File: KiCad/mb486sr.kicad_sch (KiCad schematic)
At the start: 0 parts

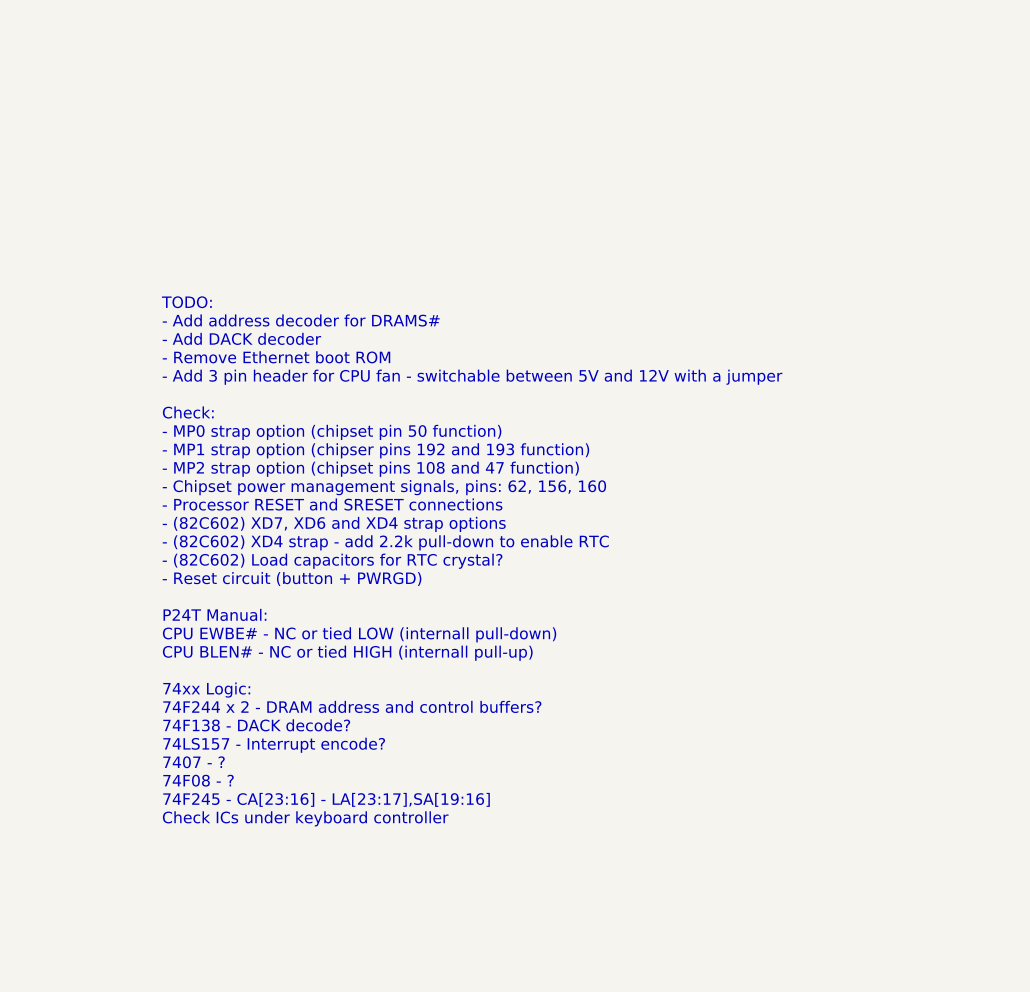
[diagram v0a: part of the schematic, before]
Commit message: Version 0.2: Update cache schematic
Signed-off-by: Sergey Kiselev <sergey.kiselev@intel.com>
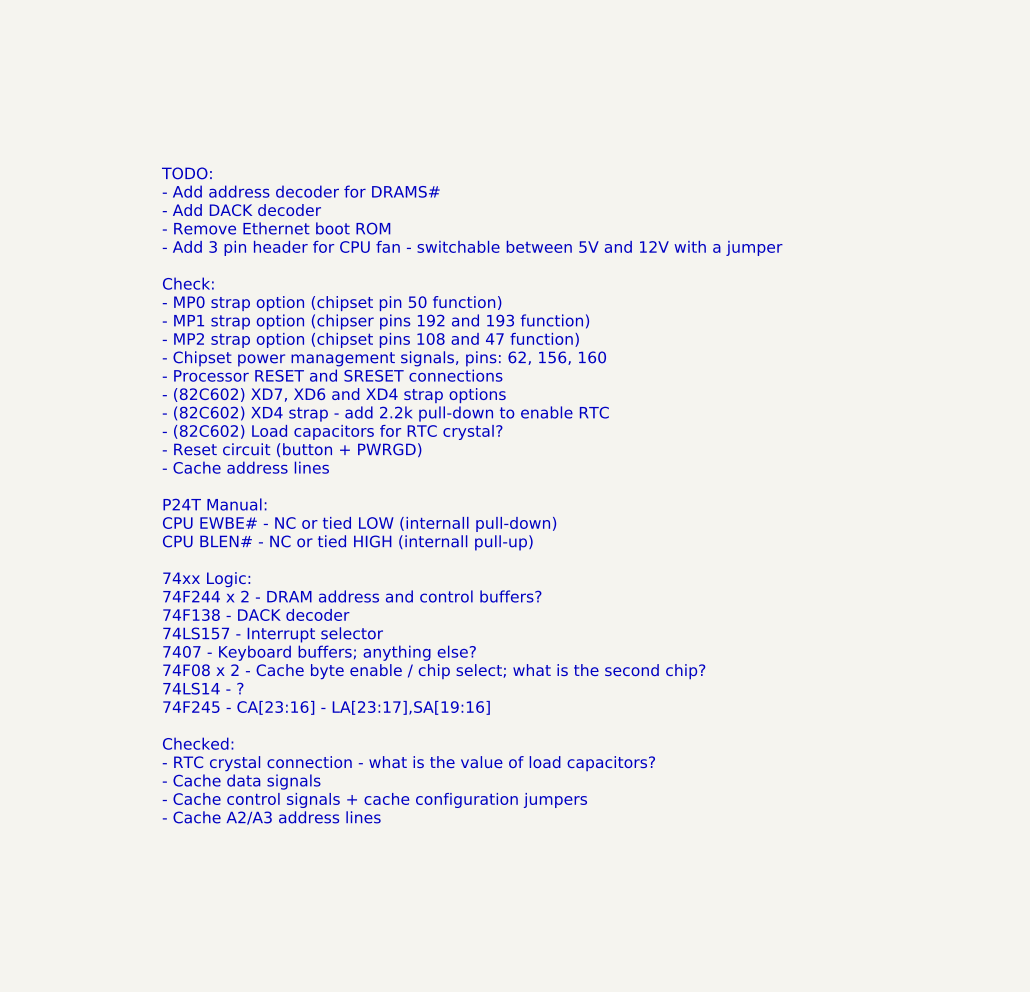
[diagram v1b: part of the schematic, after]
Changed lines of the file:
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@@
     (title "486 Sandy River Motherboard")
   )
-  (text "TODO:\n- Add address decoder for DRAMS#\n- Add DACK decoder\n- Remove Ethernet boot ROM\n- Add 3 pin header for CPU fan - switchable between 5V and 12V with a jumper\n\nCheck:\n- MP0 strap option (chipset pin 50 function)\n- MP1 strap option (chipser pins 192 and 193 function)\n- MP2 strap option (chipset pins 108 and 47 function)\n- Chipset power management signals, pins: 62, 156, 160\n- Processor RESET and SRESET connections\n- (82C602) XD7, XD6 and XD4 strap options \n- (82C602) XD4 strap - add 2.2k pull-down to enable RTC\n- (82C602) Load capacitors for RTC crystal?\n- Reset circuit (button + PWRGD)\n\nP24T Manual:\nCPU EWBE# - NC or tied LOW (internall pull-down)\nCPU BLEN# - NC or tied HIGH (internall pull-up)\n\n74xx Logic:\n74F244 x 2 - DRAM address and control buffers?\n74F138 - DACK decode?\n74LS157 - Interrupt encode?\n7407 - ?\n74F08 - ?\n74F245 - CA[23:16] - LA[23:17],SA[19:16]\nCheck ICs under keyboard controller"
+  (text "TODO:\n- Add address decoder for DRAMS#\n- Add DACK decoder\n- Remove Ethernet boot ROM\n- Add 3 pin header for CPU fan - switchable between 5V and 12V with a jumper\n\nCheck:\n- MP0 strap option (chipset pin 50 function)\n- MP1 strap option (chipser pins 192 and 193 function)\n- MP2 strap option (chipset pins 108 and 47 function)\n- Chipset power management signals, pins: 62, 156, 160\n- Processor RESET and SRESET connections\n- (82C602) XD7, XD6 and XD4 strap options \n- (82C602) XD4 strap - add 2.2k pull-down to enable RTC\n- (82C602) Load capacitors for RTC crystal?\n- Reset circuit (button + PWRGD)\n- Cache address lines\n\nP24T Manual:\nCPU EWBE# - NC or tied LOW (internall pull-down)\nCPU BLEN# - NC or tied HIGH (internall pull-up)\n\n74xx Logic:\n74F244 x 2 - DRAM address and control buffers?\n74F138 - DACK decoder\n74LS157 - Interrupt selector\n7407 - Keyboard buffers; anything else?\n74F08 x 2 - Cache byte enable / chip select; what is the second chip?\n74LS14 - ?\n74F245 - CA[23:16] - LA[23:17],SA[19:16]\n\nChecked:\n- RTC crystal connection - what is the value of load capacitors?\n- Cache data signals\n- Cache control signals + cache configuration jumpers\n- Cache A2/A3 address lines"
     (at 152.4 127 0)
     (effects (font (size 1.27 1.27)) (justify left bottom))
@@
       (reference "#PWR0154") (unit 1) (value "VCC") (footprint "")
     )
+    (path "/00000000-0000-0000-0000-000064106181/1a6e030b-bd9d-4492-beaf-de8546171e7c"
+      (reference "#PWR0155") (unit 1) (value "GND") (footprint "")
+    )
+    (path "/00000000-0000-0000-0000-000064106181/43366b22-1206-4971-a726-7a7a1dc13084"
+      (reference "#PWR0156") (unit 1) (value "GND") (footprint "")
+    )
     (path "/00000000-0000-0000-0000-000064106181/00000000-0000-0000-0000-0000621b2276"
       (reference "#PWR0157") (unit 1) (value "GND") (footprint "")
@@
       (reference "#PWR0172") (unit 1) (value "VCC") (footprint "")
     )
+    (path "/00000000-0000-0000-0000-0000639ce028/b545dce1-9c85-4083-ac19-a759d5c9f99f"
+      (reference "#PWR0173") (unit 1) (value "GND") (footprint "")
+    )
     (path "/00000000-0000-0000-0000-000064106181/7eb153c5-8a4d-4bbe-902a-62017e3bbe18"
       (reference "#PWR0174") (unit 1) (value "GND") (footprint "")
@@
       (reference "#PWR0180") (unit 1) (value "VCC") (footprint "")
     )
+    (path "/00000000-0000-0000-0000-0000639ce028/dcadb763-230c-4ef5-9a4f-6bc7914bff86"
+      (reference "#PWR0181") (unit 1) (value "VCC") (footprint "")
+    )
+    (path "/00000000-0000-0000-0000-0000639ce028/6c0dc626-6e42-4e9b-b909-af60f301c6b6"
+      (reference "#PWR0182") (unit 1) (value "VCC") (footprint "")
+    )
     (path "/00000000-0000-0000-0000-0000638712fb/00000000-0000-0000-0000-000063bb7eaf"
       (reference "#PWR0183") (unit 1) (value "GND") (footprint "")
@@
       (reference "#PWR0208") (unit 1) (value "VCC") (footprint "")
     )
-    (path "/00000000-0000-0000-0000-0000639ce028/00000000-0000-0000-0000-000063feb0c4"
+    (path "/00000000-0000-0000-0000-0000639ce028/b5d3a120-7ec7-46e4-9cca-0e75416c29e0"
       (reference "#PWR0209") (unit 1) (value "VCC") (footprint "")
     )
-    (path "/00000000-0000-0000-0000-0000639ce028/00000000-0000-0000-0000-000064077974"
+    (path "/00000000-0000-0000-0000-0000639ce028/a55e1e24-e8fe-4fd9-bac2-33d54adcc119"
       (reference "#PWR0210") (unit 1) (value "VCC") (footprint "")
     )
@@
       (reference "C90") (unit 1) (value "22uF") (footprint "Capacitor_Tantalum_SMD:CP_EIA-3528-15_AVX-H_Pad1.50x2.35mm_HandSolder")
     )
+    (path "/00000000-0000-0000-0000-000064106181/ff74cc83-255e-44fb-ae6b-1610ba9da117"
+      (reference "C101") (unit 1) (value "5pF") (footprint "")
+    )
+    (path "/00000000-0000-0000-0000-000064106181/aeb48718-394e-4854-9128-4a0de3018dbb"
+      (reference "C102") (unit 1) (value "5pF") (footprint "")
+    )
     (path "/00000000-0000-0000-0000-0000655ddd04/00000000-0000-0000-0000-000065755911"
       (reference "C121") (unit 1) (value "47pF") (footprint "")
@@
       (reference "JP53") (unit 1) (value "Ready?!") (footprint "")
     )
-    (path "/00000000-0000-0000-0000-0000639ce028/00000000-0000-0000-0000-000063f89394"
-      (reference "JP801") (unit 1) (value "32K/8K Tag IC Size") (footprint "")
+    (path "/00000000-0000-0000-0000-0000639ce028/00000000-0000-0000-0000-00006436a88a"
+      (reference "JP801") (unit 1) (value "One/Two Cache Banks") (footprint "")
     )
     (path "/00000000-0000-0000-0000-0000639ce028/00000000-0000-0000-0000-00006407732b"
-      (reference "JP802") (unit 1) (value "32K/8K Cache IC Size") (footprint "")
-    )
-    (path "/00000000-0000-0000-0000-0000639ce028/00000000-0000-0000-0000-000063e2a379"
-      (reference "JP803") (unit 1) (value "One/Two Cache Banks") (footprint "")
-    )
-    (path "/00000000-0000-0000-0000-0000639ce028/00000000-0000-0000-0000-00006436a88a"
-      (reference "JP804") (unit 1) (value "One/Two Cache Banks") (footprint "")
+      (reference "JP802") (unit 1) (value "8K/32K or 16K  Tag Size") (footprint "")
+    )
+    (path "/00000000-0000-0000-0000-0000639ce028/ed48052a-b2cf-4888-8b4e-443e953eb653"
+      (reference "JP803") (unit 1) (value "Cache A18") (footprint "")
+    )
+    (path "/00000000-0000-0000-0000-0000639ce028/c8e0883d-245d-49ca-bf3d-1ef01dac9e54"
+      (reference "JP804") (unit 1) (value "Cache A17") (footprint "")
+    )
+    (path "/00000000-0000-0000-0000-0000639ce028/36ca0365-6df4-4965-9b39-ab00d06eec83"
+      (reference "JP805") (unit 1) (value "Cache A16") (footprint "")
     )
     (path "/00000000-0000-0000-0000-000066b27913/00000000-0000-0000-0000-0000684ea034"
@@
       (reference "R652") (unit 1) (value "1k") (footprint "")
     )
+    (path "/00000000-0000-0000-0000-0000639ce028/c05d0ee7-36ff-4cb5-880f-853151621155"
+      (reference "R801") (unit 1) (value "10k") (footprint "")
+    )
+    (path "/00000000-0000-0000-0000-0000639ce028/14f60101-3e04-463e-849c-69bc2ce34821"
+      (reference "R802") (unit 1) (value "10k") (footprint "")
+    )
+    (path "/00000000-0000-0000-0000-0000639ce028/83cad221-38bb-4be4-b050-4641d249842b"
+      (reference "R803") (unit 1) (value "10k") (footprint "")
+    )
+    (path "/00000000-0000-0000-0000-0000639ce028/d043ff89-469a-45a8-931b-464c1388540a"
+      (reference "R804") (unit 1) (value "22") (footprint "")
+    )
+    (path "/00000000-0000-0000-0000-0000639ce028/5b16d7cd-0a5b-4436-afed-8dea69449887"
+      (reference "R805") (unit 1) (value "22") (footprint "")
+    )
+    (path "/00000000-0000-0000-0000-0000639ce028/e7938a44-3bcf-48fb-a9eb-29d3dc35dcbe"
+      (reference "R806") (unit 1) (value "10") (footprint "")
+    )
+    (path "/00000000-0000-0000-0000-0000639ce028/e090f588-bbd1-4bcd-92a7-48e83e17bd5f"
+      (reference "R807") (unit 1) (value "1k") (footprint "")
+    )
     (path "/00000000-0000-0000-0000-0000639b00c7/00000000-0000-0000-0000-000065ce02ef"
       (reference "RN1") (unit 1) (value "4.7k") (footprint "Resistor_THT:R_Array_SIP9")
@@
       (reference "RN305") (unit 1) (value "33") (footprint "")
     )
+    (path "/00000000-0000-0000-0000-0000639ce028/216e8e71-c4bc-413a-8ccc-4e62e6c5f5ab"
+      (reference "RN801") (unit 1) (value "22") (footprint "")
+    )
+    (path "/00000000-0000-0000-0000-0000639ce028/fb9ec19f-22b1-4348-817d-bcf78672cbc3"
+      (reference "RN802") (unit 1) (value "22") (footprint "")
+    )
+    (path "/00000000-0000-0000-0000-0000639ce028/ede12275-3708-4d01-9850-72ebb0d44367"
+      (reference "RN803") (unit 1) (value "22") (footprint "")
+    )
     (path "/00000000-0000-0000-0000-0000638712fb/00000000-0000-0000-0000-000064e3bb5e"
       (reference "SW1") (unit 1) (value "POWER") (footprint "")
@@
       (reference "U810") (unit 5) (value "74F08") (footprint "")
     )
-    (path "/00000000-0000-0000-0000-0000639ce028/00000000-0000-0000-0000-0000641b7d1f"
-      (reference "U811") (unit 1) (value "74F125") (footprint "")
-    )
-    (path "/00000000-0000-0000-0000-0000639ce028/00000000-0000-0000-0000-0000641b8931"
-      (reference "U811") (unit 2) (value "74F125") (footprint "")
-    )
     (path "/00000000-0000-0000-0000-0000638712fb/00000000-0000-0000-0000-000063929431"

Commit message: Version 0.3: Update DRAM schematic, pull-ups/pull-downs, CPU configuration jumpers
Signed-off-by: Sergey Kiselev <skiselev@gmail.com>
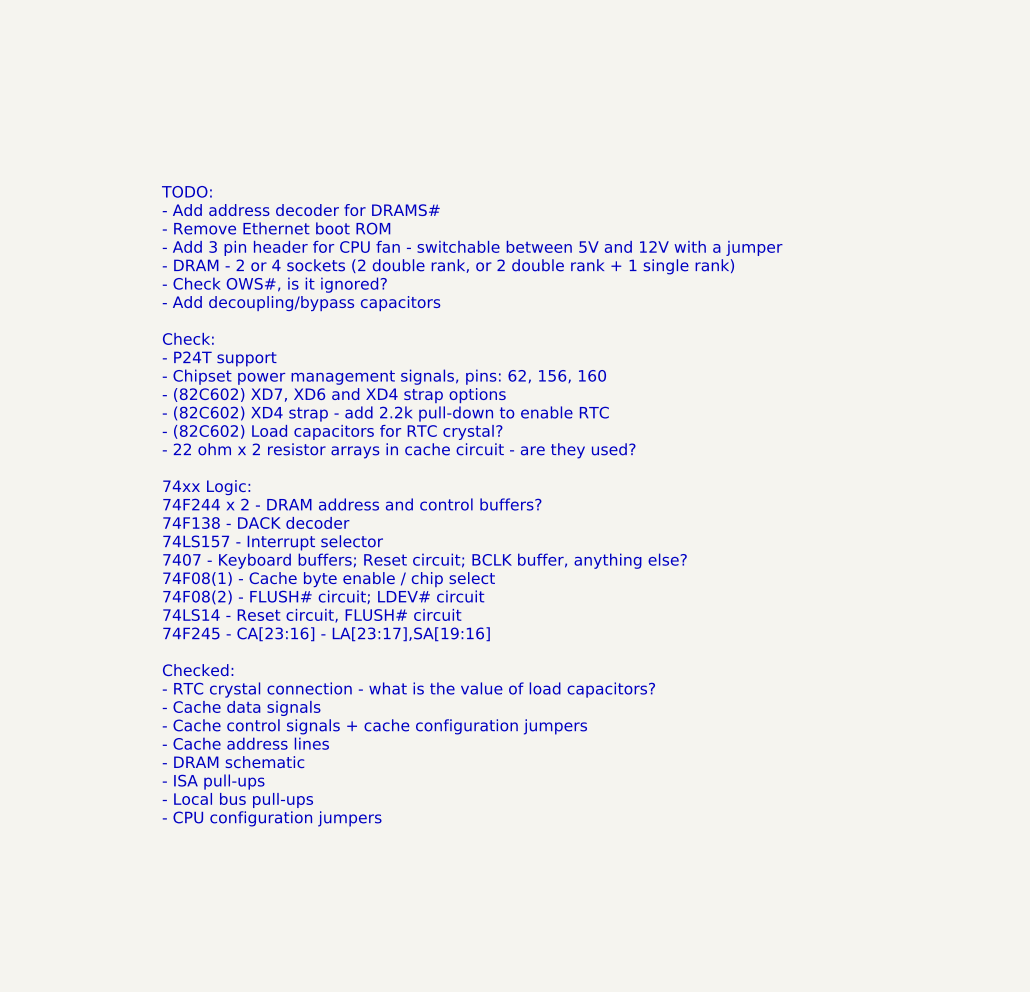
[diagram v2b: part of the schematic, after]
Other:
- note added: "TODO: - Add address decoder for DRAMS# - Remove Ethernet boot ROM - Add 3 pin header for CPU fan - switchable between 5V and 12V with a jumper - DRAM - 2 or 4 sockets (2 double rank, or 2 double rank + 1 single rank) - Check OWS#, is it ignored? - Add decoupling/bypass capacitors Check: - P24T support - Chipset power management signals, pins: 62, 156, 160 - (82C602) XD7, XD6 and XD4 strap options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"
- note removed: "TODO: - Add address decoder for DRAMS# - Add DACK decoder - Remove Ethernet boot ROM - Add 3 pin header for CPU fan - switchable between 5V and 12V with a jumper Check: - MP0 strap option (chipset pin 50 function) - MP1 strap option (chipser pins 192 and 193 function) - MP2 strap option (chipset pins 108 and 47 function) - Chipset power management signals, pins: 62, 156, 160 - Processor RESET and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"

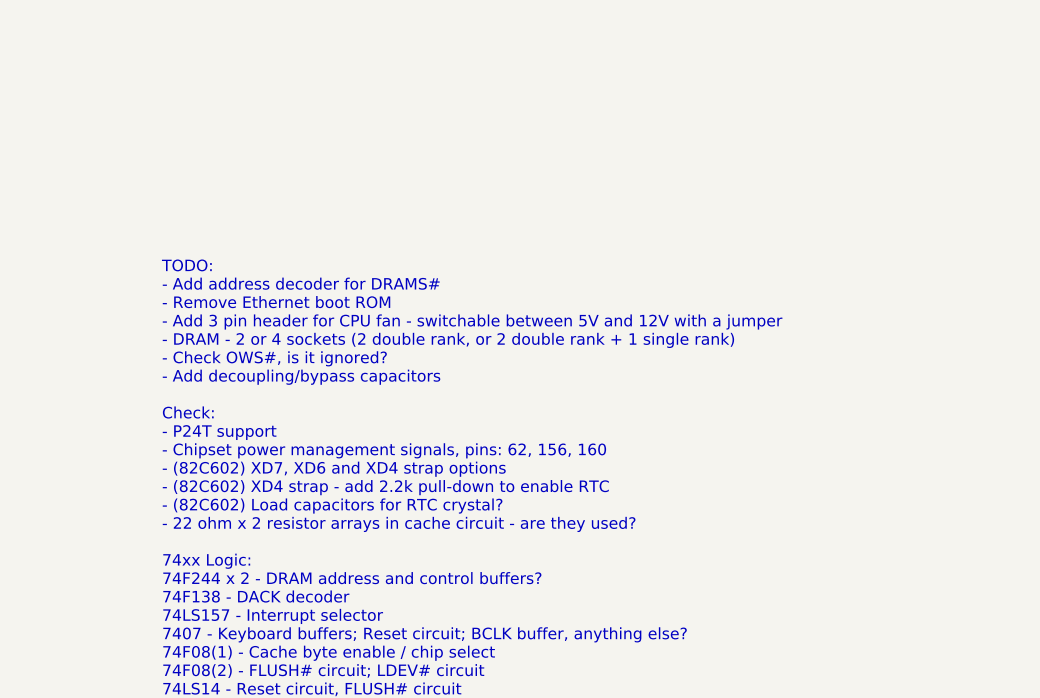
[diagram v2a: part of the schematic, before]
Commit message: Version 0.4: Update chipset connection
Signed-off-by: Sergey Kiselev <skiselev@gmail.com>
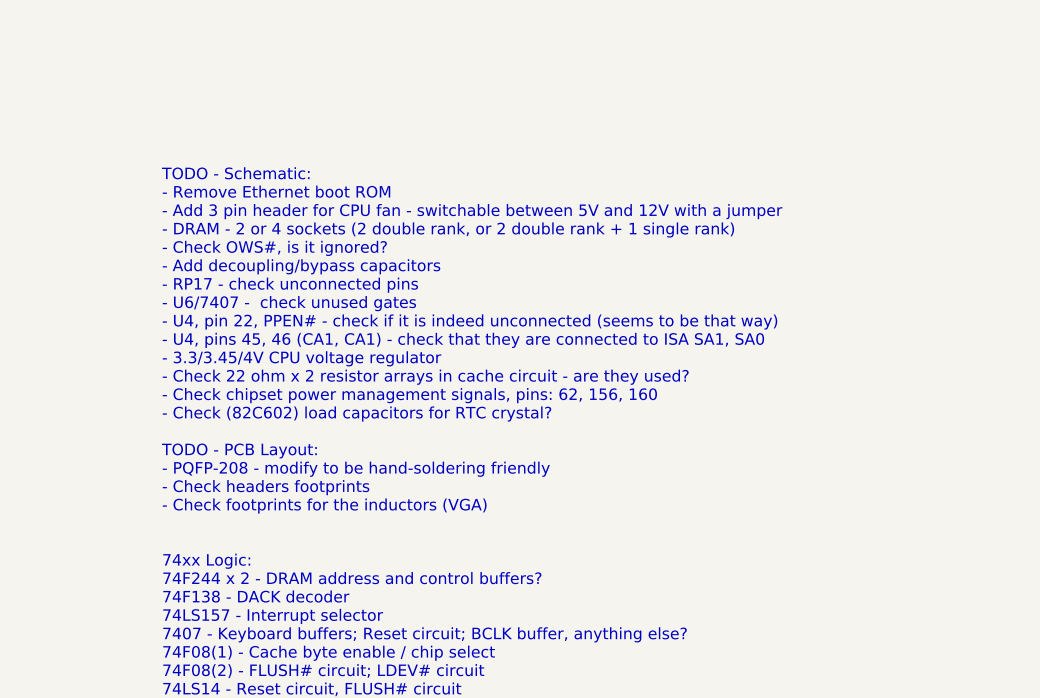
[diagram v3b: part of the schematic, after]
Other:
- note added: "TODO - Schematic: - Remove Ethernet boot ROM - Add 3 pin header for CPU fan - switchable between 5V and 12V with a jumper - DRAM - 2 or 4 sockets (2 double rank, or 2 double rank + 1 single rank) - Check OWS#, is it ignored? - Add decoupling/bypass capacitors - RP17 - check unconnected pins - U6/7407 - check unused gates - U4, pin 22, PPEN# - check if it is indeed unconnected (seems to be that wa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"
- note removed: "TODO: - Add address decoder for DRAMS# - Remove Ethernet boot ROM - Add 3 pin header for CPU fan - switchable between 5V and 12V with a jumper - DRAM - 2 or 4 sockets (2 double rank, or 2 double rank + 1 single rank) - Check OWS#, is it ignored? - Add decoupling/bypass capacitors Check: - P24T support - Chipset power management signals, pins: 62, 156, 160 - (82C602) XD7, XD6 and XD4 strap options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"

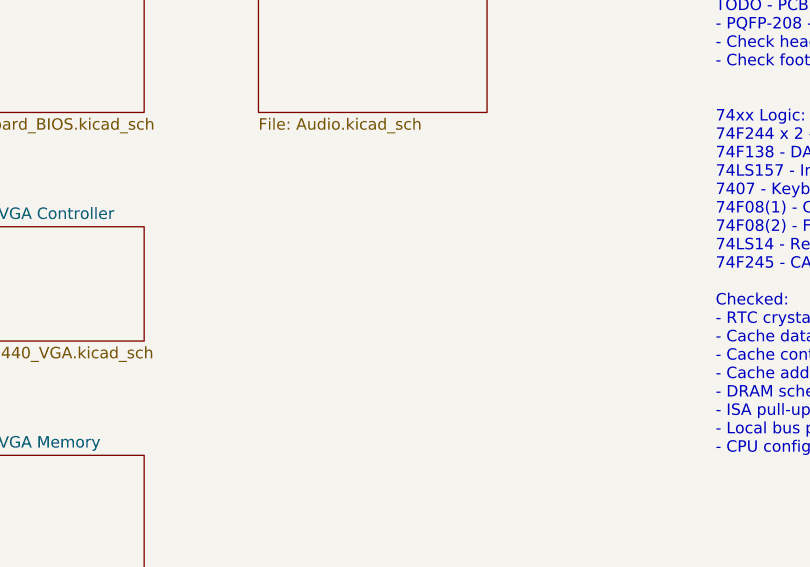
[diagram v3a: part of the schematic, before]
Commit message: More schematic updates. Remove old KiCad files
Signed-off-by: Sergey Kiselev <skiselev@gmail.com>
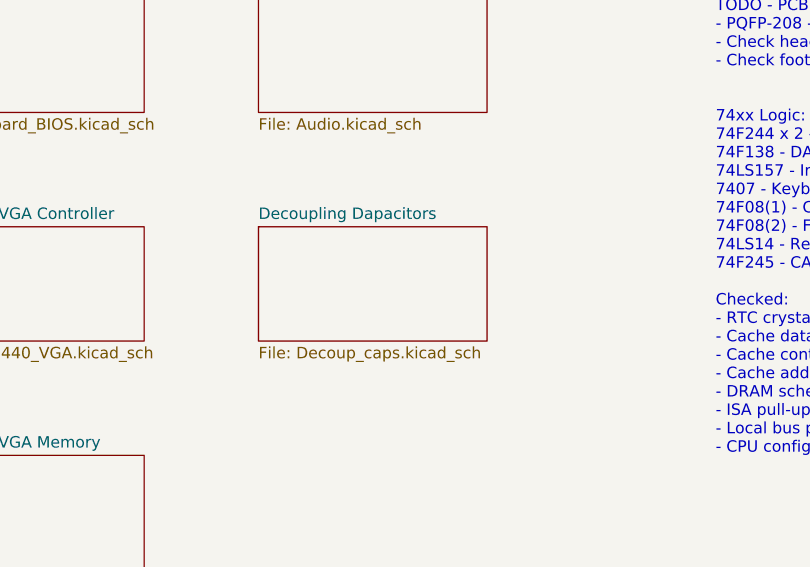
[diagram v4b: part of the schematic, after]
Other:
- added sheet Decoupling Dapacitors (Decoup_caps.kicad_sch)
